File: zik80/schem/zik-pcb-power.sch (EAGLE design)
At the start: 12 parts, among them IC1 TPS7133QP, IC2 7805TV, IC3 TPS7133QP

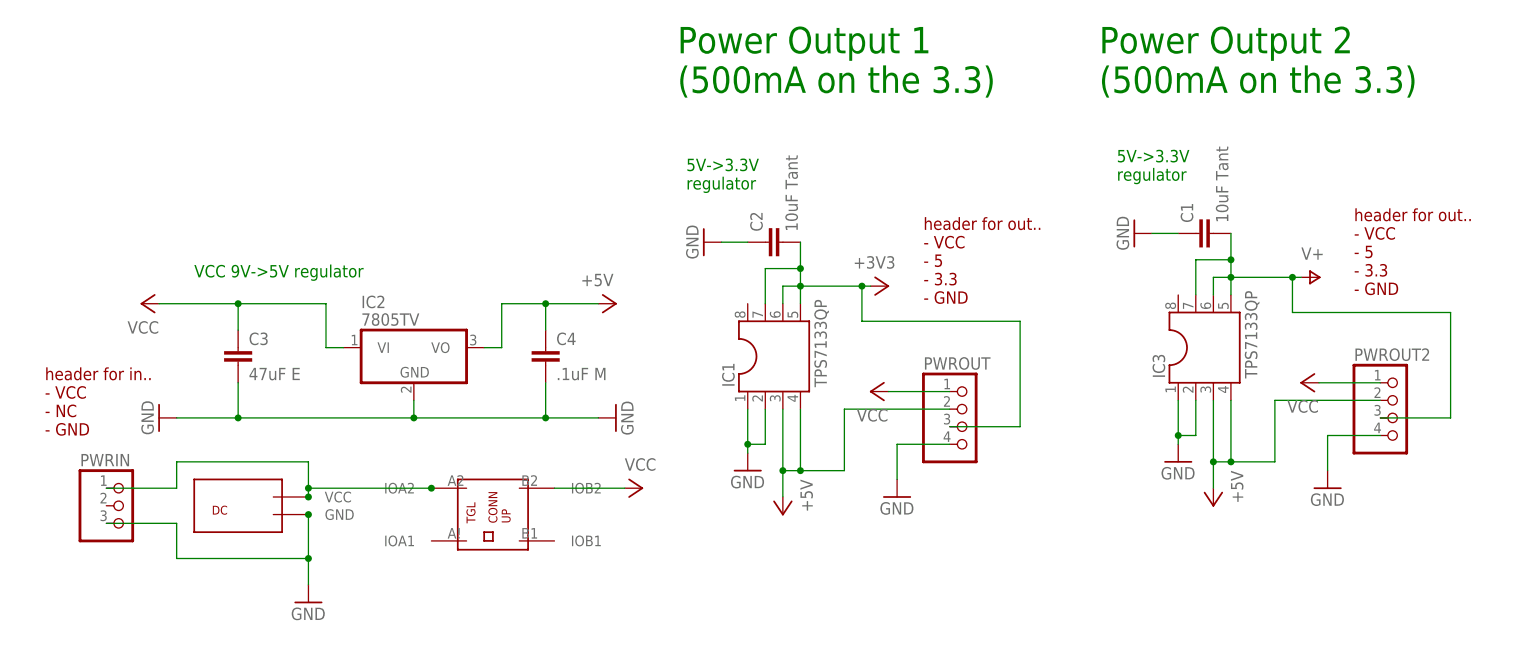
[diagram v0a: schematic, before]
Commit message: few mods to the power pcb schem; finalizing the gpu pcb schem; started power pcb board layout.. woowoo!
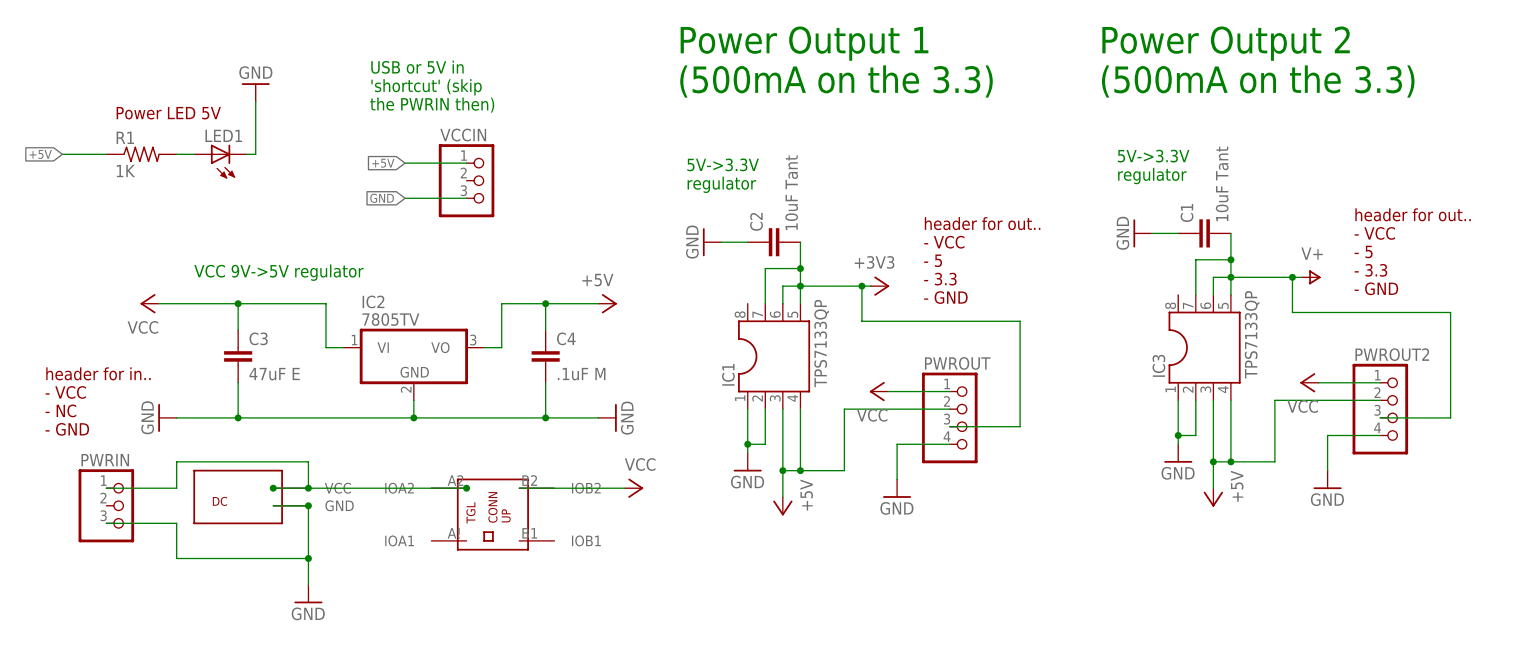
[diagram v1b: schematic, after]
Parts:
- added LED1: (no value), SparkFun-LED:LED5MM
- added R1: 1K, rcl:R-US_0207/10
- added VCCIN: (no value), pinhead:PINHD-1X3
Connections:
- new net N$3: LED1.A, R1.2
- net +5V: now also R1.1, VCCIN.1
- net GND: now also LED1.C, U$1.GND, VCCIN.3
- net N$1: now also U$1.VCC, U$2.IOA2
- net VCC: now also U$2.IOB2
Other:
- note added: "Power LED 5V"
- note added: "USB or 5V in 'shortcut' (skip the PWRIN then)"
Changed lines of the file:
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@@
 <layer number="48" name="Document" color="7" fill="1" visible="no" active="no"/>
 <layer number="49" name="Reference" color="7" fill="1" visible="no" active="no"/>
+<layer number="50" name="dxf" color="7" fill="1" visible="no" active="no"/>
 <layer number="51" name="tDocu" color="7" fill="1" visible="no" active="no"/>
 <layer number="52" name="bDocu" color="7" fill="1" visible="no" active="no"/>
+<layer number="53" name="tGND_GNDA" color="7" fill="9" visible="no" active="no"/>
+<layer number="54" name="bGND_GNDA" color="1" fill="9" visible="no" active="no"/>
+<layer number="56" name="wert" color="7" fill="1" visible="no" active="no"/>
+<layer number="57" name="tCAD" color="10" fill="1" visible="no" active="no"/>
+<layer number="58" name="bCAD" color="11" fill="1" visible="no" active="no"/>
 <layer number="91" name="Nets" color="2" fill="1" visible="yes" active="yes"/>
 <layer number="92" name="Busses" color="1" fill="1" visible="yes" active="yes"/>
@@
 <layer number="97" name="Info" color="7" fill="1" visible="yes" active="yes"/>
 <layer number="98" name="Guide" color="6" fill="1" visible="yes" active="yes"/>
+<layer number="100" name="Muster" color="7" fill="1" visible="no" active="no"/>
+<layer number="101" name="Patch_Top" color="12" fill="4" visible="yes" active="yes"/>
+<layer number="102" name="Vscore" color="7" fill="1" visible="yes" active="yes"/>
+<layer number="103" name="tMap" color="7" fill="1" visible="no" active="yes"/>
+<layer number="104" name="Name" color="7" fill="1" visible="yes" active="yes"/>
+<layer number="105" name="tPlate" color="7" fill="1" visible="no" active="yes"/>
+<layer number="106" name="bPlate" color="7" fill="1" visible="no" active="yes"/>
+<layer number="107" name="Crop" color="7" fill="1" visible="no" active="yes"/>
+<layer number="108" name="tplace-old" color="10" fill="1" visible="yes" active="yes"/>
+<layer number="109" name="ref-old" color="11" fill="1" visible="yes" active="yes"/>
+<layer number="116" name="Patch_BOT" color="9" fill="4" visible="yes" active="yes"/>
+<layer number="121" name="_tsilk" color="7" fill="1" visible="yes" active="yes"/>
+<layer number="122" name="_bsilk" color="7" fill="1" visible="yes" active="yes"/>
+<layer number="125" name="_tNames" color="7" fill="1" visible="no" active="yes"/>
+<layer number="144" name="Drill_legend" color="7" fill="1" visible="no" active="yes"/>
+<layer number="151" name="HeatSink" color="7" fill="1" visible="yes" active="yes"/>
+<layer number="199" name="Contour" color="7" fill="1" visible="yes" active="yes"/>
+<layer number="200" name="200bmp" color="1" fill="10" visible="no" active="no"/>
+<layer number="201" name="201bmp" color="2" fill="1" visible="no" active="no"/>
+<layer number="202" name="202bmp" color="3" fill="1" visible="no" active="no"/>
+<layer number="203" name="203bmp" color="4" fill="10" visible="no" active="yes"/>
+<layer number="204" name="204bmp" color="5" fill="10" visible="no" active="yes"/>
+<layer number="205" name="205bmp" color="6" fill="10" visible="no" active="yes"/>
+<layer number="206" name="206bmp" color="7" fill="10" visible="no" active="yes"/>
+<layer number="207" name="207bmp" color="8" fill="10" visible="no" active="yes"/>
+<layer number="208" name="208bmp" color="9" fill="10" visible="no" active="yes"/>
+<layer number="209" name="209bmp" color="7" fill="1" visible="no" active="yes"/>
+<layer number="210" name="210bmp" color="7" fill="1" visible="no" active="yes"/>
+<layer number="211" name="211bmp" color="7" fill="1" visible="no" active="yes"/>
+<layer number="212" name="212bmp" color="7" fill="1" visible="no" active="yes"/>
+<layer number="213" name="213bmp" color="7" fill="1" visible="no" active="yes"/>
+<layer number="214" name="214bmp" color="7" fill="1" visible="no" active="yes"/>
+<layer number="215" name="215bmp" color="7" fill="1" visible="no" active="yes"/>
+<layer number="216" name="216bmp" color="7" fill="1" visible="no" active="yes"/>
+<layer number="217" name="217bmp" color="18" fill="1" visible="no" active="no"/>
+<layer number="218" name="218bmp" color="19" fill="1" visible="no" active="no"/>
+<layer number="219" name="219bmp" color="20" fill="1" visible="no" active="no"/>
+<layer number="220" name="220bmp" color="21" fill="1" visible="no" active="no"/>
+<layer number="221" name="221bmp" color="22" fill="1" visible="no" active="no"/>
+<layer number="222" name="222bmp" color="23" fill="1" visible="no" active="no"/>
+<layer number="223" name="223bmp" color="24" fill="1" visible="no" active="no"/>
+<layer number="224" name="224bmp" color="25" fill="1" visible="no" active="no"/>
+<layer number="250" name="Descript" color="3" fill="1" visible="no" active="no"/>
+<layer number="251" name="SMDround" color="12" fill="11" visible="no" active="no"/>
+<layer number="254" name="cooling" color="7" fill="1" visible="yes" active="yes"/>
 </layers>
 <schematic xreflabel="%F%N/%S.%C%R" xrefpart="/%S.%C%R">
@@
 <part name="P+7" library="supply1" deviceset="VCC" device=""/>
 <part name="P+8" library="supply1" deviceset="V+" device=""/>
+<part name="VCCIN" library="pinhead" deviceset="PINHD-1X3" device=""/>
+<part name="LED1" library="SparkFun-LED" deviceset="LED" device="5MM"/>
+<part name="R1" library="rcl" deviceset="R-US_" device="0207/10" value="1K"/>
+<part name="GND12" library="supply1" deviceset="GND" device=""/>
 </parts>
 <sheets>
@@
 <text x="133.35" y="50.8" size="3.81" layer="91">Power Output 2
 (500mA on the 3.3)</text>
+<text x="27.94" y="48.26" size="1.778" layer="91">USB or 5V in
+'shortcut' (skip
+the PWRIN then)</text>
+<text x="-8.89" y="46.99" size="1.778" layer="94">Power LED 5V</text>
 </plain>
 <instances>
@@
 <instance part="GND5" gate="1" x="63.5" y="3.81" rot="R90"/>
 <instance part="P+3" gate="VCC" x="-5.08" y="20.32" rot="R90"/>
-<instance part="U$1" gate="G$1" x="2.54" y="-12.7"/>
+<instance part="U$1" gate="G$1" x="2.54" y="-11.43"/>
 <instance part="U$2" gate="G$1" x="50.8" y="-15.24" rot="R90"/>
 <instance part="P+5" gate="VCC" x="67.31" y="-6.35" rot="R270"/>
@@
 <instance part="P+7" gate="VCC" x="162.56" y="8.89" rot="R90"/>
 <instance part="P+8" gate="1" x="165.1" y="24.13" rot="R270"/>
+<instance part="VCCIN" gate="A" x="44.45" y="38.1"/>
+<instance part="LED1" gate="G$1" x="5.08" y="41.91" rot="R90"/>
+<instance part="R1" gate="G$1" x="-5.08" y="41.91"/>
+<instance part="GND12" gate="1" x="11.43" y="52.07" rot="R180"/>
 </instances>
 <busses>
@@
 <pinref part="PWROUT2" gate="A" pin="2"/>
 <wire x1="158.75" y1="6.35" x2="173.99" y2="6.35" width="0.1524" layer="91"/>
+</segment>
+<segment>
+<pinref part="VCCIN" gate="A" pin="1"/>
+<wire x1="41.91" y1="40.64" x2="33.02" y2="40.64" width="0.1524" layer="91"/>
+<label x="33.02" y="40.64" size="1.27" layer="95" rot="R180" xref="yes"/>
+</segment>
+<segment>
+<pinref part="R1" gate="G$1" pin="1"/>
+<wire x1="-16.51" y1="41.91" x2="-10.16" y2="41.91" width="0.1524" layer="91"/>
+<label x="-16.51" y="41.91" size="1.27" layer="95" rot="R180" xref="yes"/>
 </segment>
 </net>
@@
 </segment>
 <segment>
-<wire x1="19.05" y1="-10.16" x2="19.05" y2="-16.51" width="0.1524" layer="91"/>
-<junction x="19.05" y="-10.16"/>
+<wire x1="19.05" y1="-8.89" x2="19.05" y2="-16.51" width="0.1524" layer="91"/>
+<junction x="19.05" y="-8.89"/>
 <pinref part="PWRIN" gate="A" pin="3"/>
 <wire x1="-10.16" y1="-11.43" x2="0" y2="-11.43" width="0.1524" layer="91"/>
@@
 <wire x1="19.05" y1="-20.32" x2="19.05" y2="-16.51" width="0.1524" layer="91"/>
 <junction x="19.05" y="-16.51"/>
+<pinref part="U$1" gate="G$1" pin="GND"/>
+<wire x1="19.05" y1="-8.89" x2="13.97" y2="-8.89" width="0.1524" layer="91"/>
+</segment>
+<segment>
+<pinref part="VCCIN" gate="A" pin="3"/>
+<wire x1="41.91" y1="35.56" x2="33.02" y2="35.56" width="0.1524" layer="91"/>
+<label x="33.02" y="35.56" size="1.27" layer="95" rot="R180" xref="yes"/>
+</segment>
+<segment>
+<pinref part="LED1" gate="G$1" pin="C"/>
+<wire x1="10.16" y1="41.91" x2="11.43" y2="41.91" width="0.1524" layer="91"/>
+<wire x1="11.43" y1="41.91" x2="11.43" y2="49.53" width="0.1524" layer="91"/>
+<pinref part="GND12" gate="1" pin="GND"/>
 </segment>
 </net>
@@
 </segment>
 <segment>
-<wire x1="54.61" y1="-6.35" x2="64.77" y2="-6.35" width="0.1524" layer="91"/>
+<wire x1="49.53" y1="-6.35" x2="64.77" y2="-6.35" width="0.1524" layer="91"/>
 <pinref part="P+5" gate="VCC" pin="VCC"/>
+<pinref part="U$2" gate="G$1" pin="IOB2"/>
 </segment>
 <segment>
@@
 <net name="N$1" class="0">
 <segment>
-<wire x1="19.05" y1="-7.62" x2="19.05" y2="-6.35" width="0.1524" layer="91"/>
-<wire x1="19.05" y1="-6.35" x2="36.83" y2="-6.35" width="0.1524" layer="91"/>
-<junction x="36.83" y="-6.35"/>
-<junction x="19.05" y="-7.62"/>
+<wire x1="13.97" y1="-6.35" x2="19.05" y2="-6.35" width="0.1524" layer="91"/>
+<wire x1="19.05" y1="-6.35" x2="41.91" y2="-6.35" width="0.1524" layer="91"/>
+<junction x="41.91" y="-6.35"/>
+<junction x="13.97" y="-6.35"/>
 <pinref part="PWRIN" gate="A" pin="1"/>
 <wire x1="-10.16" y1="-6.35" x2="0" y2="-6.35" width="0.1524" layer="91"/>
@@
 <wire x1="19.05" y1="-2.54" x2="19.05" y2="-6.35" width="0.1524" layer="91"/>
 <junction x="19.05" y="-6.35"/>
+<pinref part="U$1" gate="G$1" pin="VCC"/>
+<pinref part="U$2" gate="G$1" pin="IOA2"/>
 </segment>
 </net>
@@
 </segment>
 </net>
+<net name="N$3" class="0">
+<segment>
+<pinref part="R1" gate="G$1" pin="2"/>
+<pinref part="LED1" gate="G$1" pin="A"/>
+<wire x1="0" y1="41.91" x2="2.54" y2="41.91" width="0.1524" layer="91"/>
+</segment>
+</net>
 </nets>
 </sheet>
 </sheets>
+<errors>
+</errors>
 </schematic>
 </drawing>

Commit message: Made a couple notes on power and gpu schems, of things needing correction; fiddled with vga out on real pcb.. works!
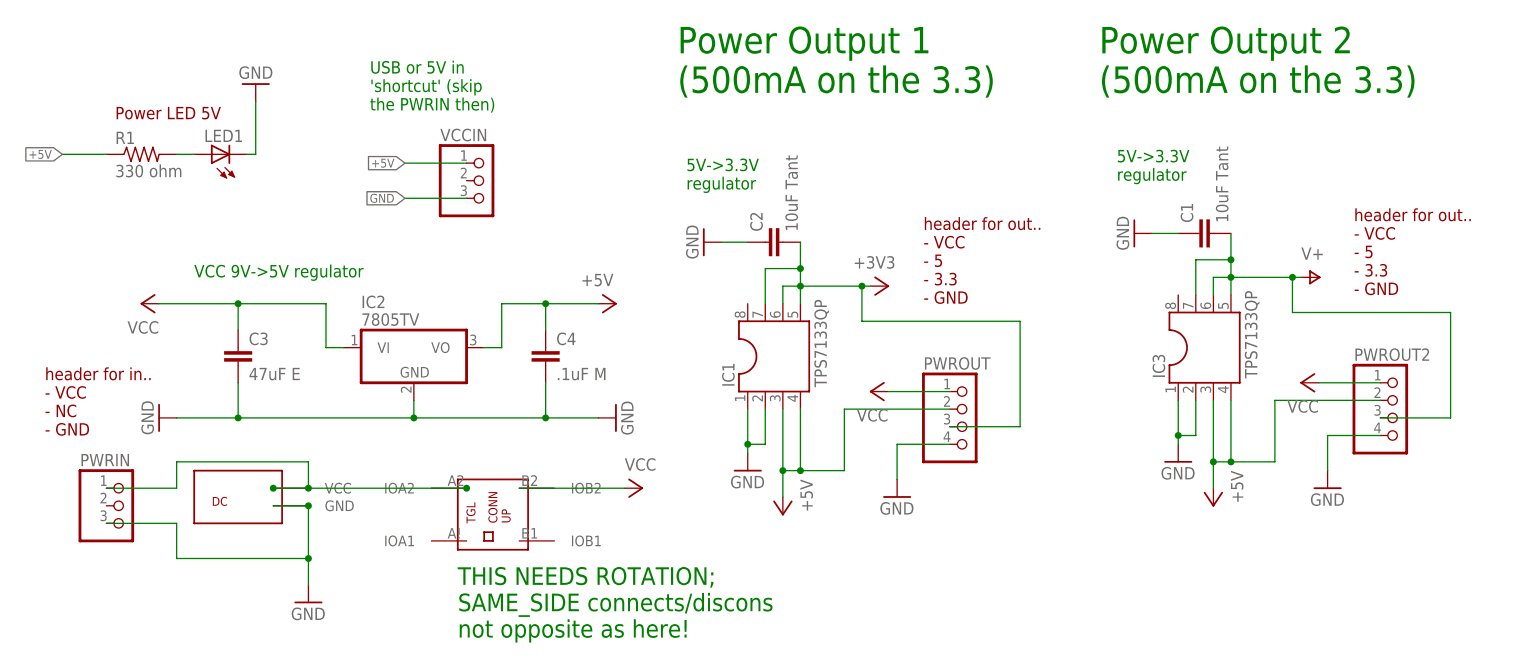
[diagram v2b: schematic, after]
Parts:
- R1: value 1K -> 330 ohm
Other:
- note added: "THIS NEEDS ROTATION; SAME_SIDE connects/discons not opposite as here!"
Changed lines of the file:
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@@
 <setting verticaltext="up"/>
 </settings>
-<grid distance="0.05" unitdist="inch" unit="inch" style="dots" multiple="1" display="yes" altdistance="0.01" altunitdist="inch" altunit="inch"/>
+<grid distance="0.1" unitdist="inch" unit="inch" style="lines" multiple="1" display="no" altdistance="0.01" altunitdist="inch" altunit="inch"/>
 <layers>
 <layer number="1" name="Top" color="4" fill="1" visible="no" active="no"/>
@@
 <part name="VCCIN" library="pinhead" deviceset="PINHD-1X3" device=""/>
 <part name="LED1" library="SparkFun-LED" deviceset="LED" device="5MM"/>
-<part name="R1" library="rcl" deviceset="R-US_" device="0207/10" value="1K"/>
+<part name="R1" library="rcl" deviceset="R-US_" device="0207/10" value="330 ohm"/>
 <part name="GND12" library="supply1" deviceset="GND" device=""/>
 </parts>
@@
 the PWRIN then)</text>
 <text x="-8.89" y="46.99" size="1.778" layer="94">Power LED 5V</text>
+<text x="40.64" y="-27.94" size="2.54" layer="91">THIS NEEDS ROTATION;
+SAME_SIDE connects/discons
+not opposite as here!</text>
 </plain>
 <instances>
